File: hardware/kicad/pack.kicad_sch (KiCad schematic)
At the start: 127 parts, among them U1 MT3608

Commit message: hardware: pack hierarchical schematic (root + 7 function sheets)
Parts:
- removed BT1, BT2, BT3, BT4: 18650, local:BatteryHolder_MYOUNG_BH-18650-A6AJ012, symbol Device:Battery_Cell
- removed C_BAT, C_PMID, C_SYS, C_VBUS: 10uF, Capacitor_SMD:C_0805_2012Metric_Pad1.18x1.45mm_HandSolder, symbol Device:C
- removed C_BTST: 47nF, Capacitor_SMD:C_0805_2012Metric_Pad1.18x1.45mm_HandSolder, symbol Device:C
- removed C_LDO1, C_LDO2: 1uF, Capacitor_SMD:C_0805_2012Metric_Pad1.18x1.45mm_HandSolder, symbol Device:C
- removed C_MCU1, C_MON1, C_MON2, C_NRST: 100nF, Capacitor_SMD:C_0805_2012Metric_Pad1.18x1.45mm_HandSolder, symbol Device:C
- removed C_MCU2, C_REGN: 4u7, Capacitor_SMD:C_0805_2012Metric_Pad1.18x1.45mm_HandSolder, symbol Device:C
- removed D_CB1, D_CB2, D_CB3, D_CB4: SS34, Diode_SMD:D_SMA, symbol Diode:SS34
- removed D_OR1, D_OR2, D_OR3, D_OR4, D_OR5: B5819W, Diode_SMD:D_SOD-123, symbol Device:D_Schottky
- removed F1, F2, F3, F4: 5A fuse, Fuse:Fuse_1206_3216Metric_Pad1.42x1.75mm_HandSolder, symbol Device:Fuse
- removed J_USB1: HC-TYPE-C-16P-01A, Connector_USB:USB_C_Receptacle_HCTL_HC-TYPE-C-16P-01A, symbol Connector:USB_C_Receptacle_USB2.0_14P
- removed LED_MCU: green, LED_SMD:LED_0805_2012Metric_Pad1.15x1.40mm_HandSolder, symbol Device:LED
- removed LED_STAT: red, LED_SMD:LED_0805_2012Metric_Pad1.15x1.40mm_HandSolder, symbol Device:LED
- removed L_CHG: 1u5, Inductor_SMD:L_1210_3225Metric_Pad1.42x2.65mm_HandSolder, symbol Device:L
- removed Q_A1, Q_A2, Q_A3, Q_A4, Q_B1, Q_B2, Q_B3, Q_B4: AO3401A, Package_TO_SOT_SMD:SOT-23, symbol Transistor_FET:AO3401A
- removed Q_N1, Q_N2, Q_N3, Q_N4: BSS138, Package_TO_SOT_SMD:SOT-23, symbol Transistor_FET:BSS138
- removed RT1, R_CC1, R_CC2: 5k1, Resistor_SMD:R_0805_2012Metric_Pad1.20x1.40mm_HandSolder, symbol Device:R
- removed RT2: 30k, Resistor_SMD:R_0805_2012Metric_Pad1.20x1.40mm_HandSolder, symbol Device:R
- removed R_ALERT, R_BOOT, R_CE, R_INT_CHG, R_NTC1, R_NTC2, R_NTC3, R_NTC4, R_PWRDN: 10k, Resistor_SMD:R_0805_2012Metric_Pad1.20x1.40mm_HandSolder, symbol Device:R
- removed R_BAT1, R_BAT2, R_SYS1: 0R, Resistor_SMD:R_1206_3216Metric_Pad1.30x1.75mm_HandSolder, symbol Device:R
- removed R_BYP1, R_BYP2, R_BYP3, R_BYP4: 0R, Resistor_SMD:R_0805_2012Metric_Pad1.20x1.40mm_HandSolder, symbol Device:R
- removed R_GS1, R_GS2, R_GS3, R_GS4: 1M, Resistor_SMD:R_0805_2012Metric_Pad1.20x1.40mm_HandSolder, symbol Device:R
- removed R_LED_MCU, R_STAT, R_SW1, R_SW2, R_SW3, R_SW4: 1k, Resistor_SMD:R_0805_2012Metric_Pad1.20x1.40mm_HandSolder, symbol Device:R
- removed R_PD1, R_PD2, R_PD3, R_PD4: 100k, Resistor_SMD:R_0805_2012Metric_Pad1.20x1.40mm_HandSolder, symbol Device:R
- removed R_SCL_INT, R_SDA_INT: 4k7, Resistor_SMD:R_0805_2012Metric_Pad1.20x1.40mm_HandSolder, symbol Device:R
- removed R_SH1, R_SH2, R_SH3, R_SH4: 10mOhm, Resistor_SMD:R_1206_3216Metric_Pad1.30x1.75mm_HandSolder, symbol Device:R
- removed R_SNSF1, R_SNSF2, R_SNSF3, R_SNSF4, R_SNSS1, R_SNSS2, R_SNSS3, R_SNSS4: 10R, Resistor_SMD:R_0805_2012Metric_Pad1.20x1.40mm_HandSolder, symbol Device:R
- removed SW_BOOT, SW_RST: TS-1088-AR02016, Button_Switch_SMD:SW_SPST_TS-1088-xR020, symbol Switch:SW_Push
- removed TH1, TH2, TH3, TH4: 10k NTC, local:NTC_Bead_P2.54mm, symbol Device:Thermistor_NTC
- removed TH_CHG: 10k NTC, Resistor_SMD:R_0805_2012Metric_Pad1.20x1.40mm_HandSolder, symbol Device:Thermistor_NTC
- removed U_CHG: BQ25601RTWR, Package_DFN_QFN:QFN-24-1EP_4x4mm_P0.5mm_EP2.6x2.6mm, symbol Battery_Management:BQ25601
- removed U_LDO: XC6206P332MR, Package_TO_SOT_SMD:SOT-23-3, symbol Regulator_Linear:XC6206PxxxMR
- removed U_MCU: STM32C071KBTx, Package_QFP:LQFP-32_7x7mm_P0.8mm, symbol MCU_ST_STM32C0:STM32C071KBTx
- removed U_MON: PAC1934T-I/JQ, Package_DFN_QFN:UQFN-16-1EP_4x4mm_P0.65mm_EP2.6x2.6mm, symbol Sensor_Energy:PAC1934x-xJQ
- added #X_CARRIER: Carrier board (J_PWR1), symbol local:Pack_Link_6
- added #X_KEY: EAO 82-6121 key switch, symbol local:Conn_W_02
- J_KEY1: symbol Connector_Generic:Conn_01x02 -> local:Conn_W_02
- J_PWR1: symbol Connector_Generic:Conn_01x06 -> local:Conn_W_06
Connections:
- net +5V: now also #X_CARRIER.4 (5V)
- net GND: now also #X_CARRIER.1 (GND), #X_CARRIER.2 (GND)
- net KEY_OUT: now also #X_KEY.2
- net SCL_EXT: now also #X_CARRIER.6 (SCL)
- net SDA_EXT: now also #X_CARRIER.5 (SDA)
- net SYS: now also #X_KEY.1
- net VBAT_SW: now also #X_CARRIER.3 (VBAT)
- no-connect marks 10 -> 1
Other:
- added sheet Cell 1 branch (18650 holder) (pack-cell1.kicad_sch)
- added sheet Cell 2 branch (18650 holder) (pack-cell2.kicad_sch)
- added sheet Cell 3 branch (18650 holder) (pack-cell3.kicad_sch)
- added sheet Cell 4 branch (18650 holder) (pack-cell4.kicad_sch)
- added sheet Cell monitoring (PAC1934), diode-OR, 3V3 LDO (pack-monitor.kicad_sch)
- added sheet STM32C071 MCU, reset/boot, status LEDs (pack-mcu.kicad_sch)
- added sheet USB-C input, BQ25601 charger (pack-charger.kicad_sch)
- note added: "Pack bring-up pads (SWD, UART, I2C)"
- note added: "XH-2"
- note added: "XH-6 to the carrier's J_PWR1"
- note removed: "Cell 1 branch"
- note removed: "Cell 2 branch"
- note removed: "Cell 3 branch"
- note removed: "Cell 4 branch"
- note removed: "Cell monitoring (PAC1934), diode-OR, 3V3 LDO"
- note removed: "Key switch, 2 A PTC, 5 V boost, J_PWR1"
- note removed: "Mounting holes and power flags"
- note removed: "STM32C071 MCU, reset/boot, test pads"
- note removed: "USB-C input, BQ25601 charger"
- title: AirsoftCounter v2 pack -> AirsoftCounter v2 pack: system
- moved on the sheet: C_IN1, C_OUT1, C_OUT2, D1, F_SYS1, H1, H2, H3, H4, J_UART1, L1, R_FB1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

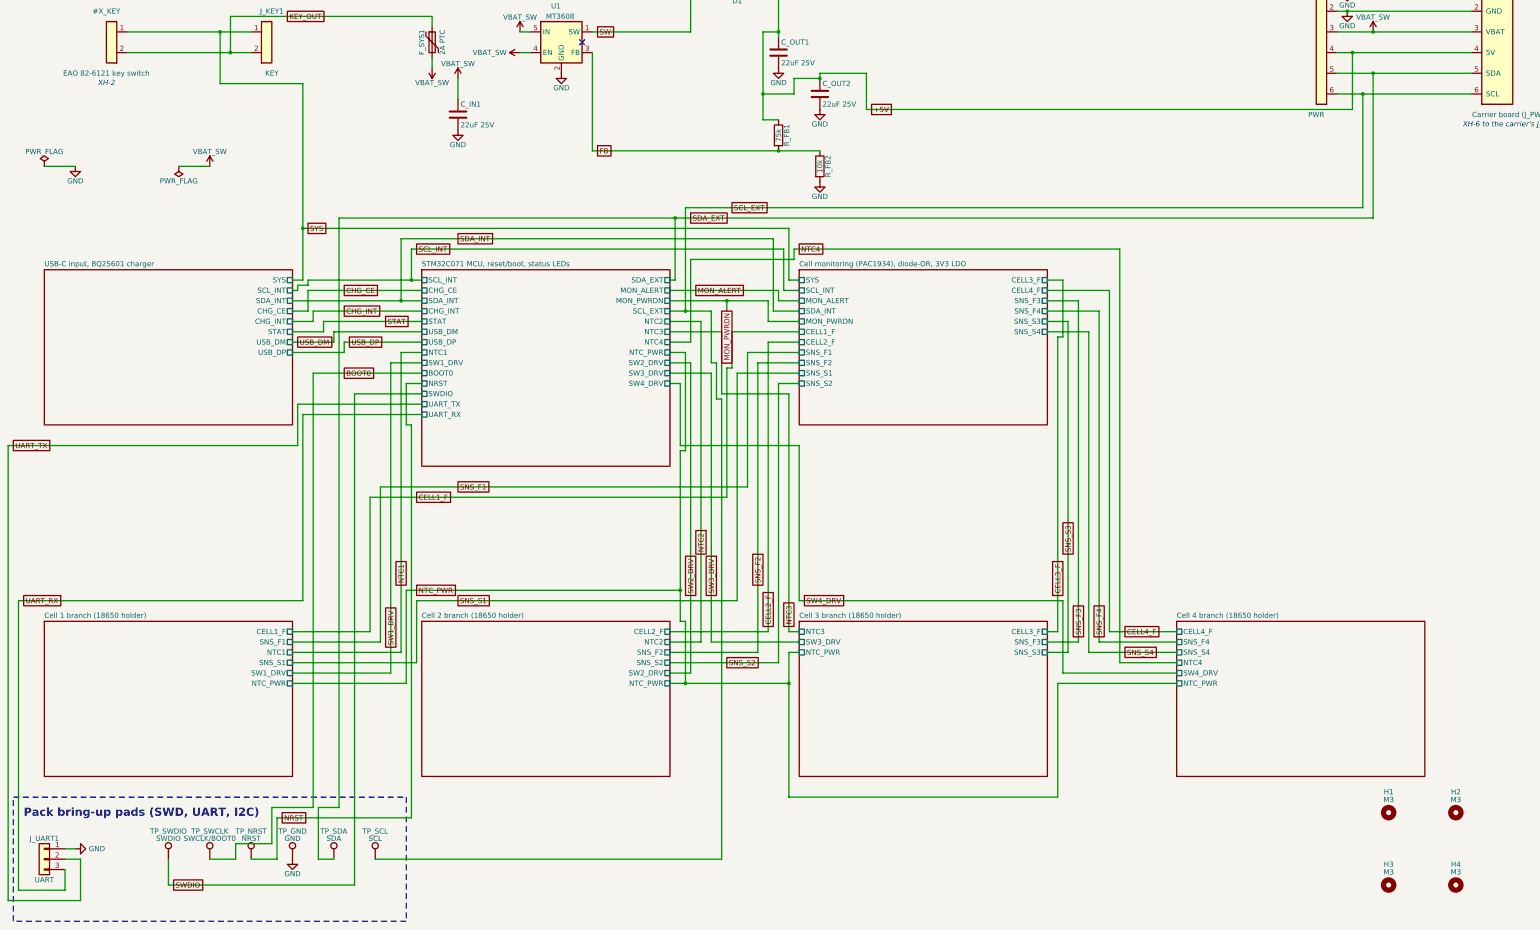
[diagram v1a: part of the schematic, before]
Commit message: hardware: pack and pack_tme hierarchical schematics
pack: root + charger, monitor, MCU and four cell sheets (7). The whole key -> PTC -> 5 V boost -> J_PWR1
chain stays on the root, because J_KEY1 and J_PWR1 are root parts and VBAT_SW has exactly one capacitor
(C_IN1). Root also carries the bring-up pads, the holes and the rail bulk caps; off-board #X_CARRIER and
#X_KEY hang off their connectors with cable notes. USB-C gets no off-board part (J_USB1 has duplicated
pins) - J_USB1 and C_VBUS stay on the charger sheet, which keeps VBUS single-file. The charger's
INT/STAT pull-ups moved to the monitor sheet, where +3V3 and its capacitors are. pack_tme derives the
same sheets with the INA226 per cell, the L072 and its own USB/charger placements.

Gates (both boards): netlist matches; all -> ERC 0, DRC 0 violations / 0 unconnected / 0 parity, gerbers
ok; pcb_diff vs 66bdf5c identical apart from footprint paths (105/127 and 111/132 path-changed);
jlc_bom/jlc_cpl/tme_bom byte-identical; review with board: pack 6 errors = 5x VPACK + 1x U_MON ~{PWRDN},
pack_tme 17 = 5x VPACK + 12x U_MON1..4 Vbus/Vin+/Vin-. Every one is a pre-existing name/structure
finding of the flat design (measured: pack flat 2, pack_tme flat 13), reported once per sheet that draws
the net - not new, and deliberately not suppressed.
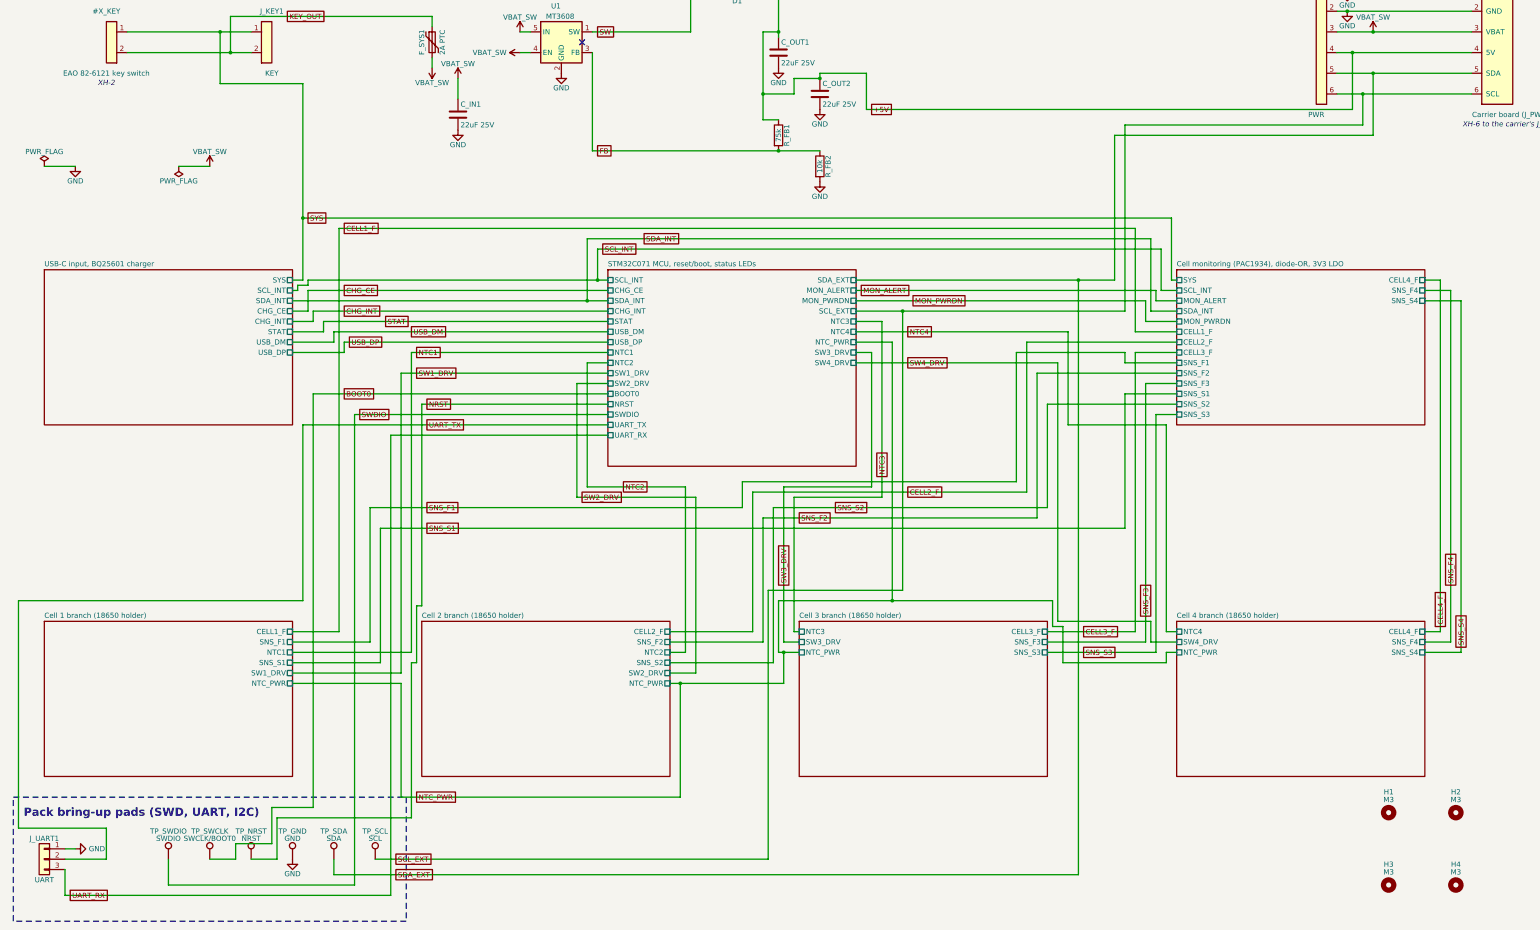
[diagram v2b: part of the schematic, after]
